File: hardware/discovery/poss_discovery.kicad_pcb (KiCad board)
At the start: 2 copper layers, 96.5 x 66 mm, 68 parts, among them CON1 USB-MICRO-B, SW1 SW_PUSH, SW10 SW_PUSH, SW11 SW_PUSH, SW12 SW_PUSH, SW13 SW_PUSH, SW14 SW_PUSH, SW15 SW_PUSH, SW16 SW_PUSH, SW17 SW_PUSH, SW18 SW_PUSH, SW19 SW_PUSH, SW2 SW_PUSH, SW20 SW_PUSH, SW21 SW_PUSH, SW22 SW_PUSH, SW3 SW_PUSH, SW4 SW_PUSH, SW5 SW_PUSH, SW6 SW_PUSH, SW7 SW_PUSH, SW8 SW_PUSH, SW9 SW_PUSH, U1 STM32F4_DISCO_Header, U2 MCP73831, U3 BD33IA5, U4 STM32F407VG

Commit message: Discovery: Add audio DAC
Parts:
- removed U1: STM32F4_DISCO_Header, stm32f4-disco:STM32F4-DISCO-HEADERS-SMD
- added C10: 1uF, Capacitors_SMD:C_0805, F.Cu at (167.6, 82.7)
- added C11: 1uF, Capacitors_SMD:C_0805, F.Cu at (170.3, 82.7)
- added C6: 0.1uF, Capacitors_SMD:C_0805, F.Cu at (173.2, 85.7)
- added C7: 0.1uF, Capacitors_SMD:C_0805, F.Cu at (173.2, 87.9)
- added C8: 0.1uF, Capacitors_SMD:C_0805, F.Cu at (164.8, 82.7)
- added C9: 0.1uF, Capacitors_SMD:C_0805, F.Cu at (169.0, 92.3)
- added U5: SGTL5000, Housings_DFN_QFN:UQFN-20-1EP_3x3mm_Pitch0.4mm, F.Cu at (168.1, 87.9)
- moved BAT1 13.6 mm to (108.2, 84.2)
- moved R2 13.6 mm to (99.3, 84.5)
- moved BT1 13.6 mm to (93.2, 83.9)
- moved C1 13.6 mm to (103.0, 81.4)
- moved CON1 13.6 mm to (115.2, 83.3)
- moved D27 13.6 mm to (115.2, 88.0)
- moved R1 13.6 mm to (106.2, 84.3)
- moved U2 13.6 mm to (103.0, 84.3)
- moved C5 10.7 mm to (162.1, 82.7), turned to 90 degrees
- moved C2 7.40 mm to (133.2, 84.8)
- moved U3 7.40 mm to (137.6, 84.8)
- moved C3 6.75 mm to (142.9, 81.9), turned to 180 degrees
- moved U4 6.56 mm to (153.5, 92.5)
- moved C4 3.99 mm to (162.8, 100.6)
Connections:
- U4 pad 29: I2S3_WS -> I2S_LRCLK
- U4 pad 34: Net-(U4-Pad34) -> ROW4
- U4 pad 64: I2S3_MCK -> I2S_MCLK
- U4 pad 78: I2S3_SCK -> I2S_SCLK
- U4 pad 79: ROW4 -> I2S_DOUT
- U4 pad 80: I2S3_SD -> I2S_DIN
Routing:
- net VIN: track 16.6 -> 0.51 mm
- net 3V3: track 3.63 -> 9.38 mm
- net Net-(C8-Pad2): track 0.00 -> 5.05 mm
- net Net-(C11-Pad2): track 0.00 -> 3.49 mm
- net Net-(C6-Pad1): track 0.00 -> 3.30 mm
- net (no net): track 0.00 -> 2.92 mm, vias 0 -> 2
- net Net-(C10-Pad2): track 0.00 -> 2.75 mm
- net Net-(C7-Pad2): track 0.00 -> 2.58 mm
- net Net-(C5-Pad1): track 3.18 -> 5.73 mm
- net Net-(C4-Pad1): track 2.78 -> 4.99 mm
- net Net-(C9-Pad2): track 0.00 -> 1.98 mm
- net GND: track 6.73 -> 7.77 mm, vias 0 -> 13
- added copper zone on F.Cu, net 3V3
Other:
- net class DAC_traces added: clearance 0.16, trace_width 0.16, via_dia 0.6, via_drill 0.4
- net class power added: clearance 0.3, trace_width 0.5, via_dia 0.6, via_drill 0.4
- rule trace_min: 0.2 -> 0.16

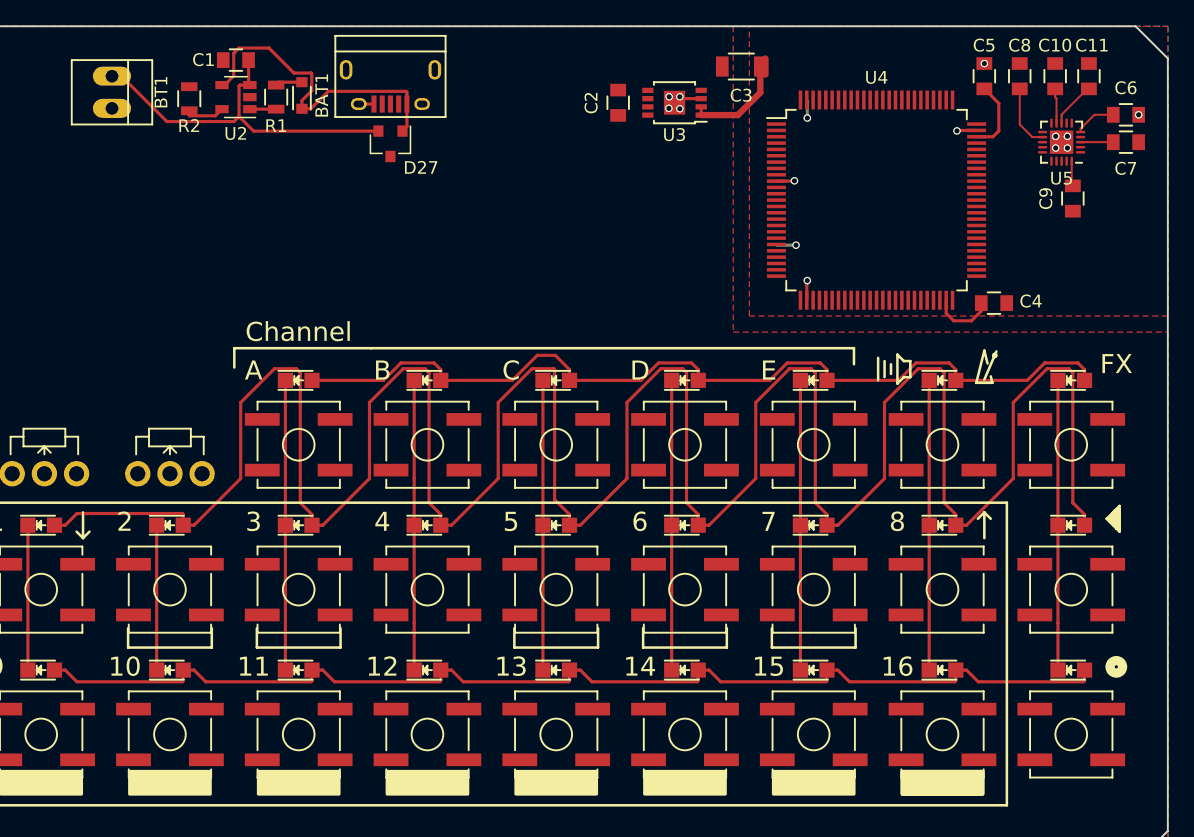
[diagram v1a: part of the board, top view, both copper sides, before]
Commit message: Discovery: Connect all button to the wakeup pin
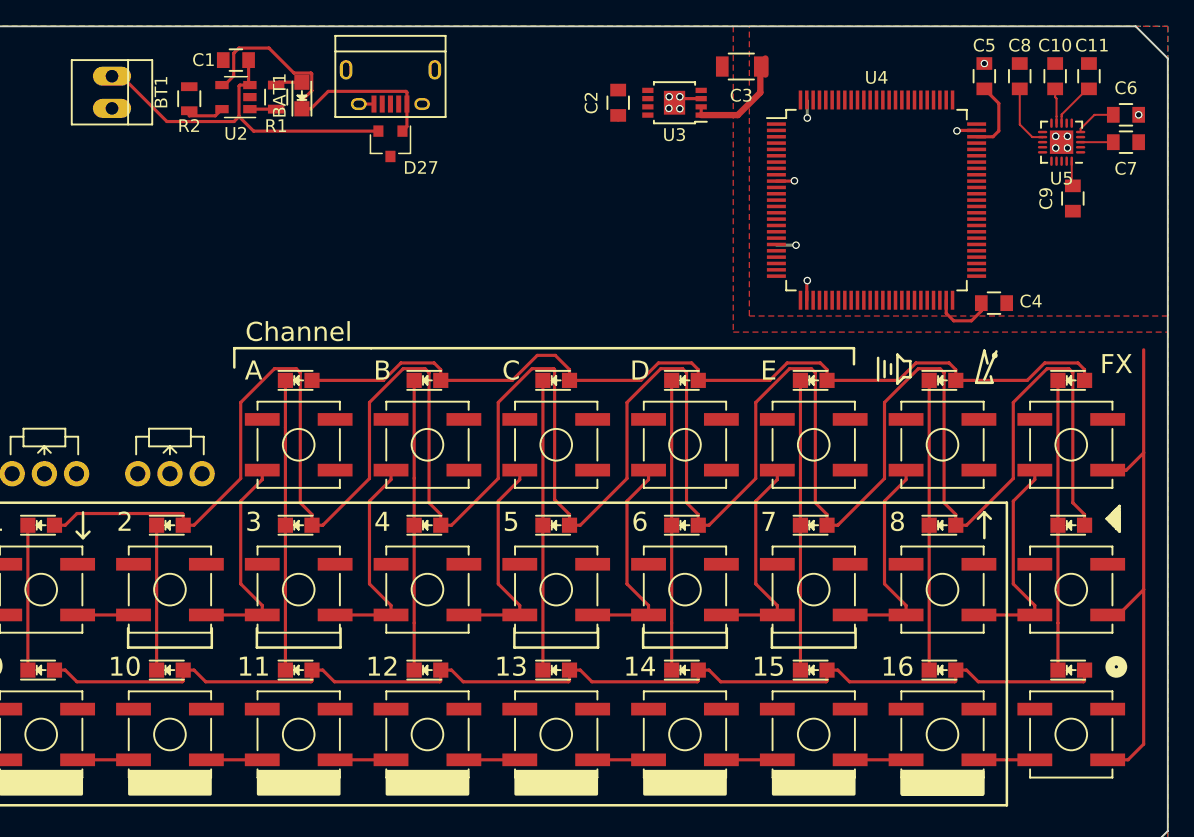
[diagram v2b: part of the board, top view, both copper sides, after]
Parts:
- BAT1: footprint Diodes_SMD:D_0805 -> LEDs:LED_0805
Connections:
- net Audio_Reset renamed Net-(U4-Pad85)
- net ROw5 renamed ROW5
- Play1 pad 2: GND -> WAKEUP
- Play2 pad 2: GND -> WAKEUP
- SW1 pad 2: GND -> WAKEUP
- SW10 pad 2: GND -> WAKEUP
- SW11 pad 2: GND -> WAKEUP
- SW12 pad 2: GND -> WAKEUP
- SW13 pad 2: GND -> WAKEUP
- SW14 pad 2: GND -> WAKEUP
- SW15 pad 2: GND -> WAKEUP
- SW16 pad 2: GND -> WAKEUP
- SW17 pad 2: GND -> WAKEUP
- SW18 pad 2: GND -> WAKEUP
- SW19 pad 2: GND -> WAKEUP
- SW2 pad 2: GND -> WAKEUP
- SW20 pad 2: GND -> WAKEUP
- SW21 pad 2: GND -> WAKEUP
- SW22 pad 2: GND -> WAKEUP
- SW3 pad 2: GND -> WAKEUP
- SW4 pad 2: GND -> WAKEUP
- SW5 pad 2: GND -> WAKEUP
- SW6 pad 2: GND -> WAKEUP
- SW7 pad 2: GND -> WAKEUP
- SW8 pad 2: GND -> WAKEUP
- SW9 pad 2: GND -> WAKEUP
- U4 pad 23: Net-(U4-Pad23) -> WAKEUP
- Write1 pad 2: GND -> WAKEUP
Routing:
- net WAKEUP: track 0.00 -> 202.0 mm

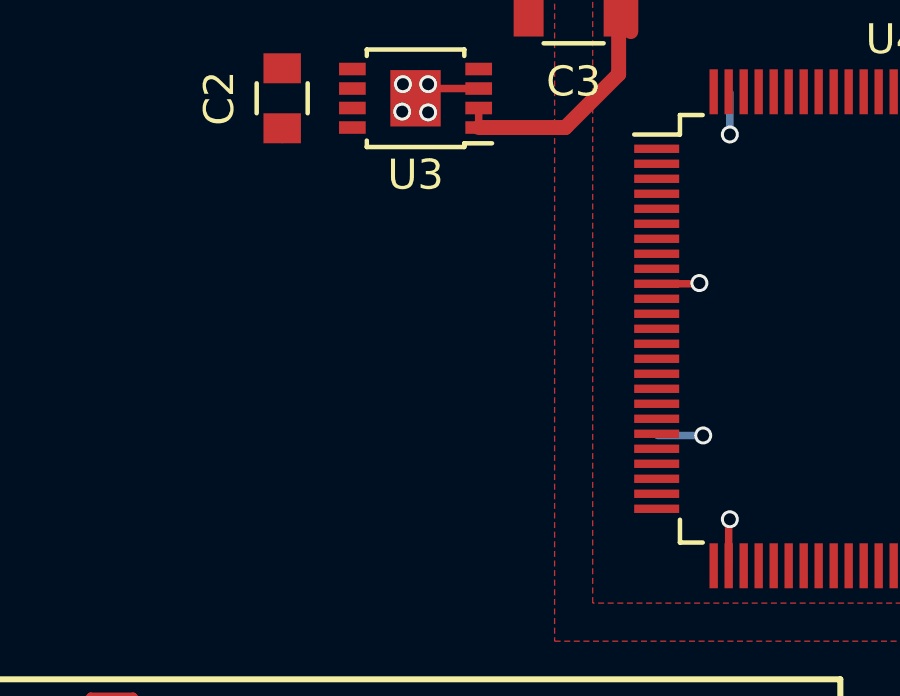
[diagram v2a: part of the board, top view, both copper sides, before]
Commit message: Discovery: add crystal
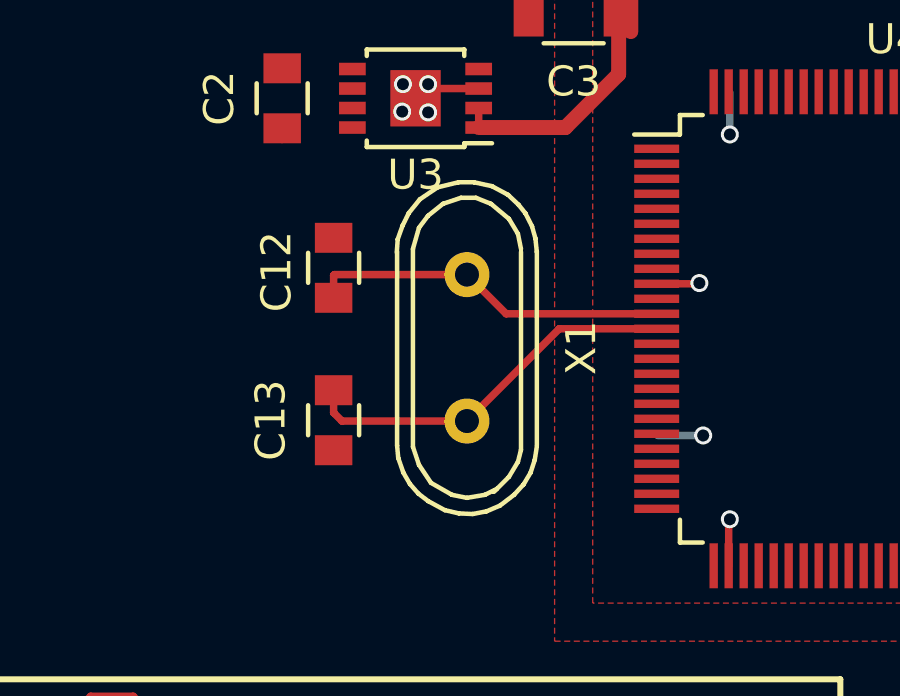
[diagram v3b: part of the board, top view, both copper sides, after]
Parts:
- added C12: C, Capacitors_SMD:C_0805, F.Cu at (134.9, 90.4)
- added C13: C, Capacitors_SMD:C_0805, F.Cu at (134.9, 95.5)
- added X1: CRYSTAL, Crystals:Crystal_HC49-U_Vertical, F.Cu at (139.3, 93.1)
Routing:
- net Net-(C13-Pad2): track 0.00 -> 12.9 mm
- net Net-(C12-Pad2): track 0.00 -> 12.1 mm

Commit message: Discovery: improve LED/button matrix layout
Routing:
- net ROW2: track 224.4 -> 106.9 mm
- net WAKEUP: track 202.0 -> 138.6 mm
- net B11: track 0.00 -> 33.4 mm, vias 0 -> 1
- net B12: track 0.00 -> 33.1 mm, vias 0 -> 1
- net B13: track 0.00 -> 32.7 mm, vias 0 -> 1
- net B14: track 0.00 -> 32.4 mm, vias 0 -> 1
- net B15: track 0.00 -> 32.3 mm, vias 0 -> 1
- net Write: track 0.00 -> 32.0 mm, vias 0 -> 1
- net B16: track 0.00 -> 31.3 mm, vias 0 -> 1
- net ROW1: track 91.4 -> 118.6 mm
- net B3: track 0.00 -> 22.1 mm, vias 0 -> 1
- net B4: track 0.00 -> 21.8 mm, vias 0 -> 1
- net B5: track 0.00 -> 21.4 mm, vias 0 -> 1
- net B7: track 0.00 -> 21.1 mm, vias 0 -> 1
- net B6: track 0.00 -> 21.1 mm, vias 0 -> 1
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
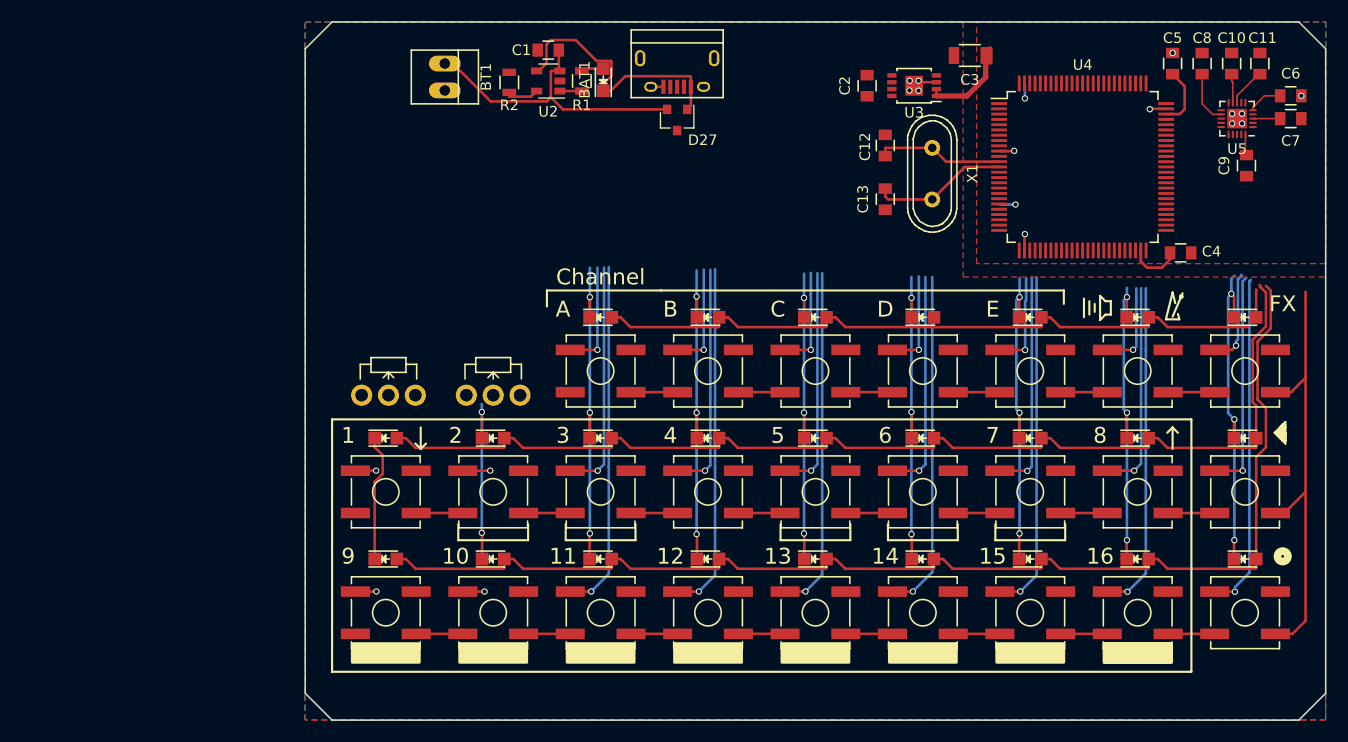
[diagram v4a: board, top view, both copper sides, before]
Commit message: Discovery: STM32F4 power a filtering
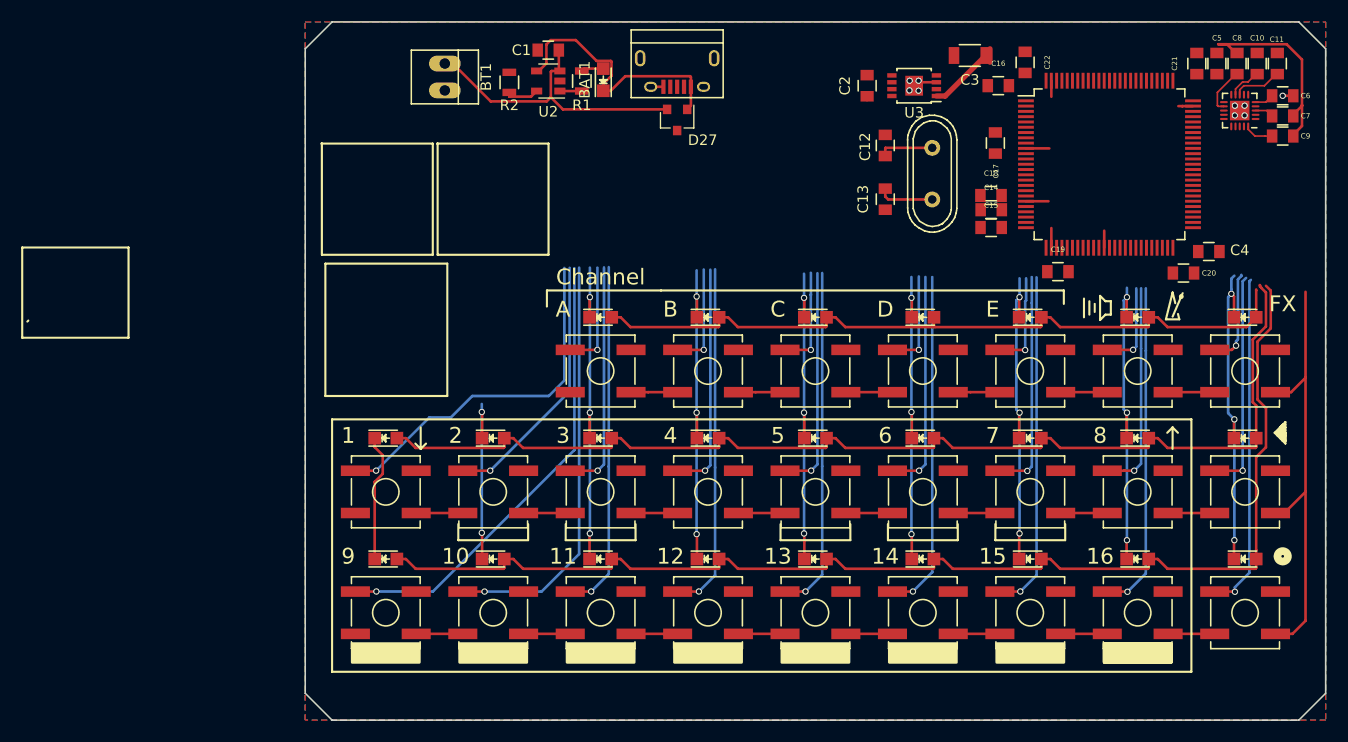
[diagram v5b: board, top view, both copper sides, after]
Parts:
- removed RV1, RV2: POT, Potentiometers:Potentiometer_WirePads_Small
- added C14: 1uF, Capacitors_SMD:C_0805, F.Cu at (144.9, 96.5)
- added C15: 0.1uF, Capacitors_SMD:C_0805, F.Cu at (144.9, 98.2)
- added C16: 22uF, Capacitors_SMD:C_0805, F.Cu at (145.6, 84.8)
- added C17: 0.1uF, Capacitors_SMD:C_0805, F.Cu at (145.3, 90.2)
- added C18: 0.1uF, Capacitors_SMD:C_0805, F.Cu at (144.9, 95.2)
- added C19: 0.1uF, Capacitors_SMD:C_0805, F.Cu at (151.2, 102.4)
- added C20: 0.1uF, Capacitors_SMD:C_0805, F.Cu at (163.1, 102.5)
- added C21: 0.1uF, Capacitors_SMD:C_0805, F.Cu at (164.3, 82.7)
- added C22: 0.1uF, Capacitors_SMD:C_0805, F.Cu at (148.1, 82.6)
- moved C9 4.42 mm to (172.5, 89.5), turned to 180 degrees
- moved C5 4.19 mm to (166.2, 82.7)
- moved C8 3.30 mm to (168.1, 82.7)
- moved C4 2.67 mm to (165.5, 100.5)
- moved U4 2.55 mm to (156.1, 92.2)
- moved C10 2.41 mm to (170.1, 82.7)
- moved C11 1.65 mm to (172.0, 82.7)
- moved C7 0.80 mm to (172.5, 87.6)
- moved U5 0.80 mm to (168.4, 87.1)
- moved C6 0.76 mm to (172.5, 85.7)
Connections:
- net ROW4 renamed Net-(U4-Pad34)
- net ROW5 renamed Net-(U4-Pad67)
- net USB_Over_Current renamed Net-(U4-Pad86)
- U4 pad 1: B13 -> Net-(U4-Pad1)
- U4 pad 100: Net-(U4-Pad100) -> 3V3
- U4 pad 11: Net-(U4-Pad11) -> 3V3
- U4 pad 15: COL5 -> Net-(U4-Pad15)
- U4 pad 16: BA -> Net-(U4-Pad16)
- U4 pad 17: BB -> Net-(U4-Pad17)
- U4 pad 18: COL4 -> Net-(U4-Pad18)
- U4 pad 19: Net-(U4-Pad19) -> 3V3
- U4 pad 21: Net-(U4-Pad21) -> Net-(C14-Pad2)
- U4 pad 22: Net-(U4-Pad22) -> Net-(C14-Pad2)
- U4 pad 24: POT1 -> Net-(U4-Pad24)
- U4 pad 25: COL3 -> Net-(U4-Pad25)
- U4 pad 26: POT2 -> Net-(U4-Pad26)
- U4 pad 28: Net-(U4-Pad28) -> 3V3
- U4 pad 3: B3 -> Net-(U4-Pad3)
- U4 pad 37: Net-(U4-Pad37) -> GND
- U4 pad 4: B12 -> Net-(U4-Pad4)
- U4 pad 5: B11 -> Net-(U4-Pad5)
- U4 pad 50: Net-(U4-Pad50) -> 3V3
- U4 pad 54: BD -> Net-(U4-Pad54)
- U4 pad 55: BC -> Net-(U4-Pad55)
- U4 pad 56: BPM_VOL -> Net-(U4-Pad56)
- U4 pad 57: BE -> Net-(U4-Pad57)
- U4 pad 58: FX -> Net-(U4-Pad58)
- U4 pad 6: Net-(U4-Pad6) -> 3V3
- U4 pad 63: COL1 -> Net-(U4-Pad63)
- U4 pad 65: ROW2 -> Net-(U4-Pad65)
- U4 pad 66: ROW1 -> Net-(U4-Pad66)
- U4 pad 69: COL2 -> Net-(U4-Pad69)
- U4 pad 7: B2 -> Net-(U4-Pad7)
- U4 pad 75: Net-(U4-Pad75) -> 3V3
- U4 pad 77: ROW3 -> Net-(U4-Pad77)
- U4 pad 8: B10 -> Net-(U4-Pad8)
- U4 pad 81: Play -> Net-(U4-Pad81)
- U4 pad 82: B8 -> Net-(U4-Pad82)
- U4 pad 83: Write -> Net-(U4-Pad83)
- U4 pad 84: B16 -> Net-(U4-Pad84)
- U4 pad 87: B7 -> Net-(U4-Pad87)
- U4 pad 88: B6 -> Net-(U4-Pad88)
- U4 pad 89: B15 -> Net-(U4-Pad89)
- U4 pad 9: B1 -> Net-(U4-Pad9)
- U4 pad 90: B14 -> Net-(U4-Pad90)
- U4 pad 91: B5 -> Net-(U4-Pad91)
- U4 pad 93: B9 -> Net-(U4-Pad93)
- U4 pad 95: B4 -> Net-(U4-Pad95)
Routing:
- net B9: track 1.99 -> 43.5 mm
- net B10: track 2.06 -> 39.6 mm
- net B1: track 1.96 -> 33.9 mm
- net B2: track 2.60 -> 24.9 mm
- net 3V3: track 9.38 -> 27.2 mm
- net Net-(C13-Pad2): track 12.9 -> 5.31 mm
- net GND: track 7.77 -> 14.9 mm, vias 13 -> 9
- net Net-(C12-Pad2): track 12.1 -> 5.20 mm
- net Net-(C5-Pad1): track 5.73 -> 0.00 mm
- net Net-(C4-Pad1): track 4.99 -> 0.00 mm
- net (no net): track 2.92 -> 0.00 mm, vias 2 -> 0
- net Net-(C6-Pad1): track 3.30 -> 1.81 mm
- net Net-(C11-Pad2): track 3.49 -> 4.63 mm
- net Net-(C9-Pad2): track 1.98 -> 2.80 mm
- net Net-(C7-Pad2): track 2.58 -> 1.77 mm
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- removed copper zone on F.Cu, net 3V3
